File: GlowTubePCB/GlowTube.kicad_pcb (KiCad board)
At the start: 2 copper layers, 87.3 x 86.3 mm, 37 parts, among them J1 Conn_01x08, Q1 MMBT2222A, Q2 MMBT2222A, Q3 AP40P05, Q4 AP40P05, SW1 SW-SMD_4P-L3.7-W3.0-P1.50-LS4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, SW2 SW-SMD_4P-L3.7-W3.0-P1.50-LS4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, U1 ESP32-WROOM-32E (4MB), U2 PW14, U3 BL1117-33CX, U4 Val**

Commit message: updated pcb design
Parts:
- SW1, SW2: value SW-SMD_4P-L3.7-W3.0-P1.50-LS4.7 -> TS-1185EC-C-D-B
- U2: value PW14 -> SN74AHCT32QPWRQ1
- U4: value Val** -> CP2102-GMR
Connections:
- Q2 pad 2: RESET -> RTS
- Q2 pad 3: RTS -> RESET
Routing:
- net RESET: track 89.6 -> 88.2 mm
- net RTS: track 18.4 -> 17.7 mm
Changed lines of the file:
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@@
       (net 49 "Net-(Q2-Pad1)") (pintype "passive"))
     (pad "2" smd roundrect (at -0.9375 0.95 90) (size 1.475 0.6) (layers "F.Cu" "F.Paste" "F.Mask") (roundrect_rratio 0.25)
-      (net 4 "RESET") (pintype "passive"))
-    (pad "3" smd roundrect (at 0.9375 0 90) (size 1.475 0.6) (layers "F.Cu" "F.Paste" "F.Mask") (roundrect_rratio 0.25)
       (net 50 "RTS") (pintype "passive"))
+    (pad "3" smd roundrect (at 0.9375 0 90) (size 1.475 0.6) (layers "F.Cu" "F.Paste" "F.Mask") (roundrect_rratio 0.25)
+      (net 4 "RESET") (pintype "passive"))
     (model "${KICAD6_3DMODEL_DIR}/Package_TO_SOT_SMD.3dshapes/SOT-23.step"
       (offset (xyz 0 0 0))
@@
     (property "Sheetfile" "GlowTube.kicad_sch")
     (property "Sheetname" "")
-    (attr exclude_from_pos_files exclude_from_bom)
+    (attr exclude_from_pos_files)
     (fp_text reference "LED1" (at 0.1524 -3.5306 unlocked) (layer "F.SilkS") hide
       (effects (font (size 1 1) (thickness 0.15)))
@@
       (effects (font (size 1 1) (thickness 0.15)))
     )
-    (fp_text value "PW14" (at 0 0) (layer "F.SilkS") hide
+    (fp_text value "SN74AHCT32QPWRQ1" (at 0 0) (layer "F.SilkS") hide
       (effects (font (size 1 1) (thickness 0.15)))
     )
@@
     (property "Sheetfile" "GlowTube.kicad_sch")
     (property "Sheetname" "")
-    (attr through_hole exclude_from_pos_files exclude_from_bom)
+    (attr through_hole exclude_from_pos_files)
     (fp_text reference "J1" (at 0 -2.77) (layer "F.SilkS") hide
       (effects (font (size 1 1) (thickness 0.15)))
@@
       (effects (font (size 1 1) (thickness 0.15)) (justify right))
     )
-    (fp_text value "Val**" (at 0 0 90) (layer "F.SilkS") hide
+    (fp_text value "CP2102-GMR" (at 0 0 90) (layer "F.SilkS") hide
       (effects (font (size 1.27 1.27) (thickness 0.15)))
     )
@@
       (effects (font (size 1 1) (thickness 0.15)))
     )
-    (fp_text value "SW-SMD_4P-L3.7-W3.0-P1.50-LS4.7" (at 0 4.75) (layer "F.Fab")
+    (fp_text value "TS-1185EC-C-D-B" (at 0 4.75) (layer "F.Fab")
       (effects (font (size 1 1) (thickness 0.15)))
     )
@@
       (effects (font (size 1 1) (thickness 0.15)))
     )
-    (fp_text value "SW-SMD_4P-L3.7-W3.0-P1.50-LS4.7" (at 0 4.75) (layer "F.Fab")
+    (fp_text value "TS-1185EC-C-D-B" (at 0 4.75) (layer "F.Fab")
       (effects (font (size 1 1) (thickness 0.15)))
     )
@@
     (property "Sheetfile" "GlowTube.kicad_sch")
     (property "Sheetname" "")
-    (attr exclude_from_pos_files exclude_from_bom)
+    (attr exclude_from_pos_files)
     (fp_text reference "LED2" (at 0.1524 3.5306 unlocked) (layer "B.SilkS") hide
       (effects (font (size 1 1) (thickness 0.15)) (justify mirror))
@@
   (segment (start 114.34 161.6874) (end 113.2042 162.8232) (width 0.16) (layer "F.Cu") (net 4))
   (segment (start 112.7268 162.8232) (end 112.01 163.54) (width 0.16) (layer "F.Cu") (net 4))
+  (segment (start 142.5591 142.21) (end 142.5572 142.2081) (width 0.16) (layer "F.Cu") (net 4))
   (segment (start 115 160.5) (end 117.48 160.5) (width 0.16) (layer "F.Cu") (net 4))
   (segment (start 151.16 114.35) (end 149.5289 112.7189) (width 0.16) (layer "F.Cu") (net 4))
-  (segment (start 143.62 145.8) (end 143.5072 145.6872) (width 0.16) (layer "F.Cu") (net 4))
   (segment (start 114.34 161.16) (end 115 160.5) (width 0.16) (layer "F.Cu") (net 4))
   (segment (start 117.48 160.5) (end 118.14 161.16) (width 0.16) (layer "F.Cu") (net 4))
   (segment (start 114.34 161.16) (end 114.34 161.6874) (width 0.16) (layer "F.Cu") (net 4))
-  (segment (start 143.5072 145.6872) (end 143.5072 144.0831) (width 0.16) (layer "F.Cu") (net 4))
+  (segment (start 143.66 142.21) (end 142.5591 142.21) (width 0.16) (layer "F.Cu") (net 4))
   (segment (start 149.5289 112.7189) (end 149.5289 110.7052) (width 0.16) (layer "F.Cu") (net 4))
   (via (at 112.01 163.54) (size 0.8) (drill 0.4) (layers "F.Cu" "B.Cu") (net 4))
-  (via (at 143.62 145.8) (size 0.8) (drill 0.4) (layers "F.Cu" "B.Cu") (net 4))
+  (via (at 143.66 142.21) (size 0.8) (drill 0.4) (layers "F.Cu" "B.Cu") (net 4))
   (via (at 151.16 114.35) (size 0.8) (drill 0.4) (layers "F.Cu" "B.Cu") (net 4))
-  (segment (start 143.62 145.8) (end 143.62 131.29) (width 0.16) (layer "B.Cu") (net 4))
-  (segment (start 150.77 124.14) (end 151.16 123.75) (width 0.16) (layer "B.Cu") (net 4))
-  (segment (start 131.03 157.06) (end 142.29 145.8) (width 0.16) (layer "B.Cu") (net 4))
-  (segment (start 143.62 131.29) (end 150.77 124.14) (width 0.16) (layer "B.Cu") (net 4))
-  (segment (start 118.49 157.06) (end 131.03 157.06) (width 0.16) (layer "B.Cu") (net 4))
-  (segment (start 142.29 145.8) (end 143.62 145.8) (width 0.16) (layer "B.Cu") (net 4))
-  (segment (start 112.01 163.54) (end 118.49 157.06) (width 0.16) (layer "B.Cu") (net 4))
+  (segment (start 143.62 131.29) (end 151.16 123.75) (width 0.16) (layer "B.Cu") (net 4))
+  (segment (start 143.66 144.43) (end 131.03 157.06) (width 0.16) (layer "B.Cu") (net 4))
   (segment (start 151.16 123.75) (end 151.16 114.35) (width 0.16) (layer "B.Cu") (net 4))
+  (segment (start 143.66 142.21) (end 143.66 144.43) (width 0.16) (layer "B.Cu") (net 4))
+  (segment (start 143.62 142.17) (end 143.62 131.29) (width 0.16) (layer "B.Cu") (net 4))
+  (segment (start 143.66 142.21) (end 143.62 142.17) (width 0.16) (layer "B.Cu") (net 4))
+  (segment (start 118.49 157.06) (end 112.01 163.54) (width 0.16) (layer "B.Cu") (net 4))
+  (segment (start 131.03 157.06) (end 118.49 157.06) (width 0.16) (layer "B.Cu") (net 4))
   (segment (start 142.5842 107.010844) (end 142.5842 108.6442) (width 0.16) (layer "F.Cu") (net 9))
   (segment (start 142.5842 108.6442) (end 143.1789 109.2389) (width 0.16) (layer "F.Cu") (net 9))
@@
   (segment (start 133.210027 151.140001) (end 136.059999 151.140001) (width 0.16) (layer "F.Cu") (net 48))
   (segment (start 140.69 146.51) (end 140.69 144.8981) (width 0.16) (layer "F.Cu") (net 48))
-  (segment (start 141.7425 143.9478) (end 141.7425 140.25) (width 0.16) (layer "F.Cu") (net 49))
   (segment (start 141.6072 144.0831) (end 141.7425 143.9478) (width 0.16) (layer "F.Cu") (net 49))
+  (segment (start 141.6072 140.3853) (end 141.7425 140.25) (width 0.16) (layer "F.Cu") (net 49))
+  (segment (start 141.6072 144.0831) (end 141.6072 140.3853) (width 0.16) (layer "F.Cu") (net 49))
   (segment (start 142.65 147.11) (end 142.65 147.0757) (width 0.16) (layer "F.Cu") (net 50))
-  (segment (start 142.5572 145.0487) (end 141.5901 146.0158) (width 0.16) (layer "F.Cu") (net 50))
-  (segment (start 142.5572 142.2081) (end 142.5572 145.0487) (width 0.16) (layer "F.Cu") (net 50))
+  (segment (start 143.5072 145.4328) (end 143.5072 144.0831) (width 0.16) (layer "F.Cu") (net 50))
+  (segment (start 141.5901 146.0158) (end 141.7059 145.9) (width 0.16) (layer "F.Cu") (net 50))
   (segment (start 137.73 153.14) (end 133.210027 153.14) (width 0.16) (layer "F.Cu") (net 50))
   (segment (start 141.39 149.64) (end 141.23 149.64) (width 0.16) (layer "F.Cu") (net 50))
   (segment (start 142.65 147.0757) (end 141.5901 146.0158) (width 0.16) (layer "F.Cu") (net 50))
   (segment (start 141.23 149.64) (end 137.73 153.14) (width 0.16) (layer "F.Cu") (net 50))
+  (segment (start 143.04 145.9) (end 143.5072 145.4328) (width 0.16) (layer "F.Cu") (net 50))
+  (segment (start 141.7059 145.9) (end 143.04 145.9) (width 0.16) (layer "F.Cu") (net 50))
   (via (at 142.65 147.11) (size 0.8) (drill 0.4) (layers "F.Cu" "B.Cu") (net 50))
   (via (at 141.39 149.64) (size 0.8) (drill 0.4) (layers "F.Cu" "B.Cu") (net 50))

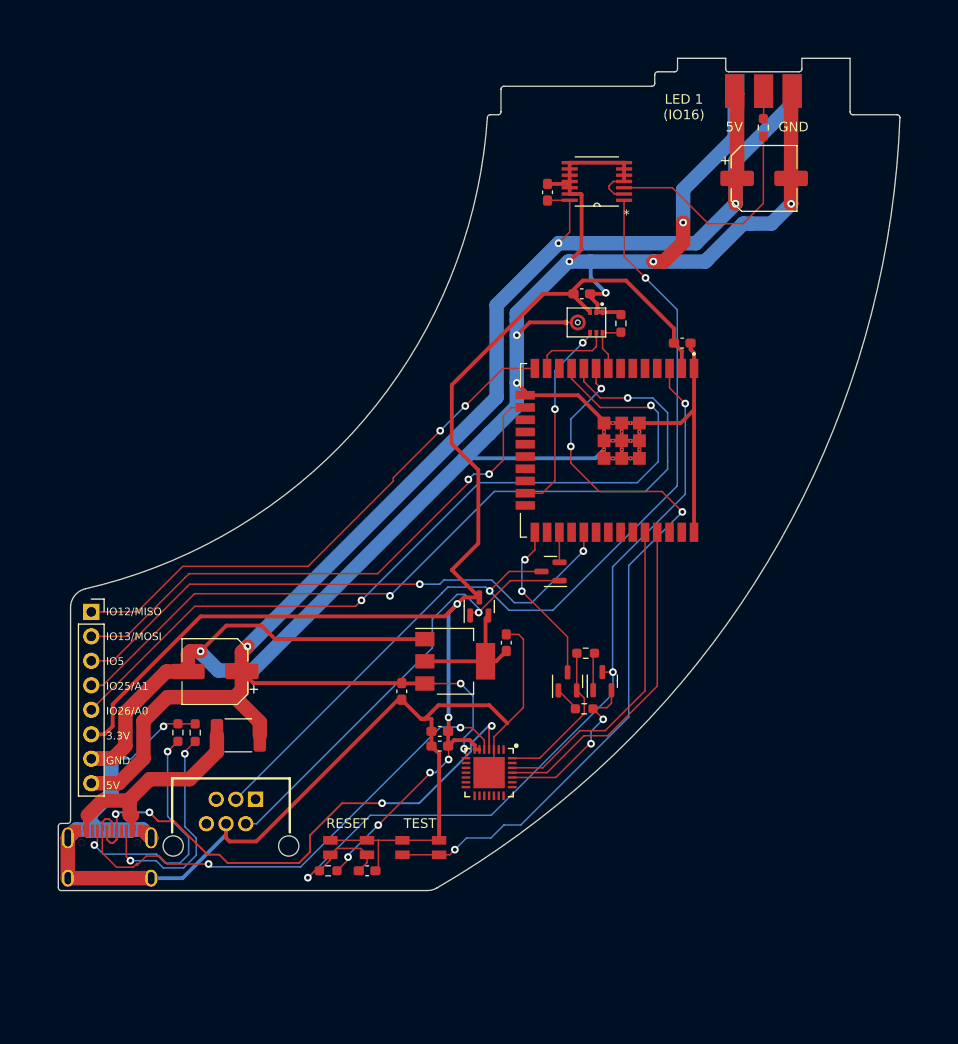
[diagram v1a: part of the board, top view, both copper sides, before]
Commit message: redesigned GlowTube PCBs
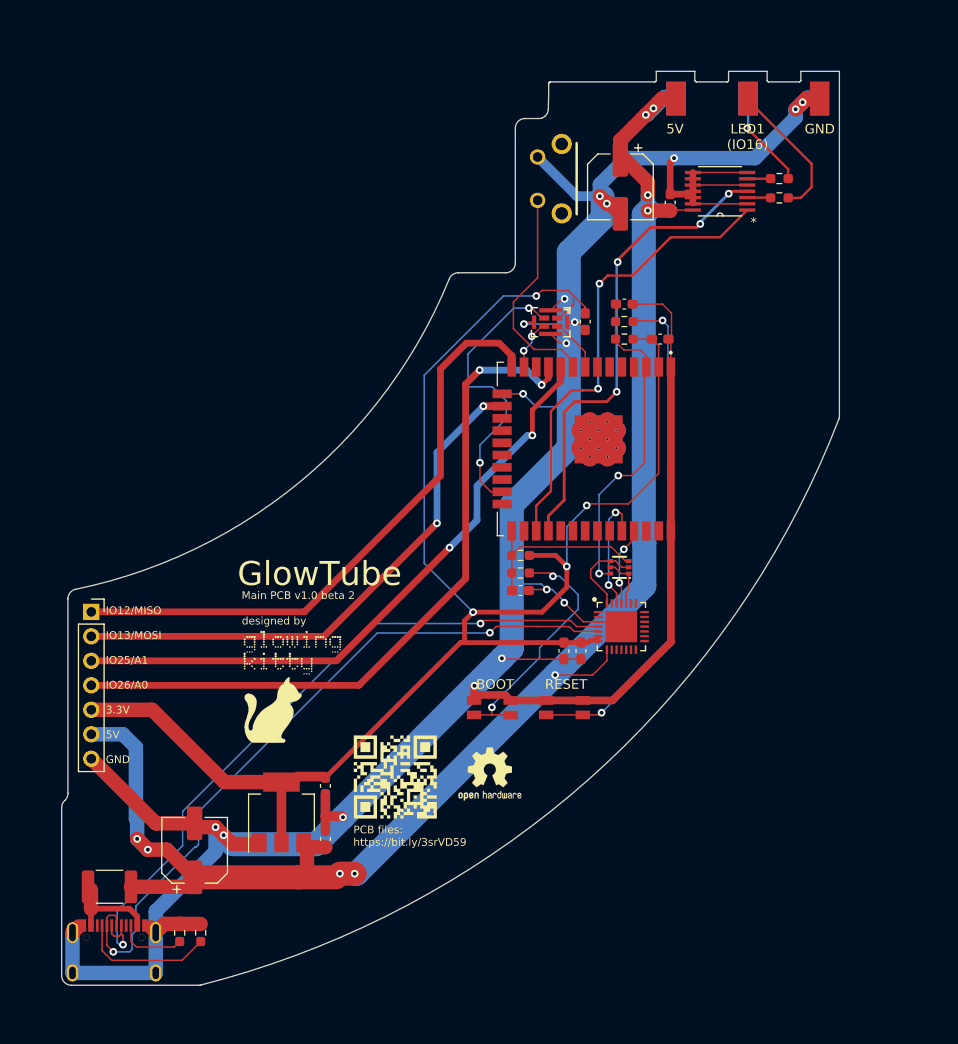
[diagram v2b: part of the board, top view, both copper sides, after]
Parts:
- removed LED1, LED2: LED_strip_contact_pads, Connector:LED strip connector pad
- removed MK1: ICS-43432, ICS-43432:MIC_ICS-43432
- removed Q1, Q2: MMBT2222A, Package_TO_SOT_SMD:SOT-23
- removed Q3, Q4: AP40P05, Package_TO_SOT_SMD:SOT-23
- removed REF**: OSHW-Logo2_7.3x6mm_SilkScreen, Symbol:OSHW-Logo2_7.3x6mm_SilkScreen
- removed RJ1: R-RJ11R06P-A800, R-RJ11R06P-A800:R-RJ11R06P-A800
- added C11: 1nF, Capacitor_SMD:C_0603_1608Metric_Pad1.08x0.95mm_HandSolder, F.Cu at (134.1, 133.7)
- added C12: KAN0637-0701B, footprint:SW-TH_KAN0637-0701B, F.Cu at (134.9, 91.0)
- added OSHW logo: OSHW-Logo2_7.3x6mm_SilkScreen, Symbol:OSHW-Logo2_7.3x6mm_SilkScreen, F.Cu at (130.9, 152.8)
- added P1: Solder_Pad, footprint:Solder pad, F.Cu at (150.3, 82.7)
- added P2: Solder_Pad, footprint:Solder pad, F.Cu at (157.8, 82.7)
- added P3: Solder_Pad, footprint:Solder pad, F.Cu at (165.2, 82.7)
- added P4: Solder_Pad, footprint:Solder pad, B.Cu at (150.1, 82.7)
- added P5: Solder_Pad, footprint:Solder pad, B.Cu at (165.0, 82.7)
- added P6: Solder_Pad, footprint:Solder pad, B.Cu at (157.6, 82.7)
- added R8: 62, Resistor_SMD:R_0603_1608Metric_Pad0.98x0.95mm_HandSolder, F.Cu at (160.9, 91.0)
- added U5: UMH3N, footprint:SC-70-6_L2.2-W1.3-P0.65-LS2.1-BR, F.Cu at (144.3, 131.3)
- added U6: GMA4030H11-F26, GMA4030H11-F26:GMA4030H11-F26, F.Cu at (137.2, 105.9)
- C1: value 220uF 10V -> 10uF; footprint Capacitor_SMD:CP_Elec_6.3x5.4 -> Capacitor_SMD:C_0603_1608Metric_Pad1.08x0.95mm_HandSolder
- C10: value 1uF -> 1nF
- C3: value 10uF -> 220uF 10V; footprint Capacitor_SMD:C_0603_1608Metric_Pad1.08x0.95mm_HandSolder -> Capacitor_SMD:CP_Elec_6.3x5.4
- C4: value 4.7uF 6.3V 10% -> 220uF 10V; footprint Capacitor_SMD:C_0603_1608Metric_Pad1.08x0.95mm_HandSolder -> Capacitor_SMD:CP_Elec_6.3x5.4
- C5: value 10uF -> 4.7uF 6.3V 10%
- C8: value 0.1uF -> 10uF
- C9: value 220uF 10V -> 0.1uF; footprint Capacitor_SMD:CP_Elec_6.3x5.4 -> Capacitor_SMD:C_0603_1608Metric_Pad1.08x0.95mm_HandSolder
- G*** (x2): moved to F.Cu
- J1: value Conn_01x08 -> Conn_01x07; footprint Connector_PinSocket_2.54mm:PinSocket_1x08_P2.54mm_Vertical -> Connector_PinSocket_2.54mm:PinSocket_1x07_P2.54mm_Vertical
- R4, R5: value 10K -> 220
- R6: value 100K -> 10K
- U1: value ESP32-WROOM-32E (4MB) -> SN74AHCT32QPWRQ1; footprint ESP32-WROOM-32E__16MB_:MODULE_ESP32-WROOM-32E_(16MB) -> SN74AHCT32QPWRQ1:SN74AHCT32QPWRQ1
- U2: value SN74AHCT32QPWRQ1 -> ESP32-WROOM-32E (4MB); footprint SN74AHCT32QPWRQ1:SN74AHCT32QPWRQ1 -> ESP32-WROOM-32E__16MB_:MODULE_ESP32-WROOM-32E_(16MB)
- U3: value BL1117-33CX -> CP2102-GMR; footprint Package_TO_SOT_SMD:SOT-223 -> CP2102-GMR:CP2102-GMR
- U4: value CP2102-GMR -> BL1117-33CX; footprint CP2102-GMR:CP2102-GMR -> Package_TO_SOT_SMD:SOT-223
- moved C10 64.6 mm to (144.8, 104.0), turned to 0 degrees
- moved C4 61.0 mm to (144.4, 91.9), turned to -90 degrees
- moved C1 57.6 mm to (148.6, 107.7)
- moved C8 57.6 mm to (113.8, 154.0), turned to 90 degrees
- moved R4 40.4 mm to (144.8, 105.8)
- moved R7 38.3 mm to (134.1, 130.1)
- moved C5 33.6 mm to (140.3, 140.0), turned to 90 degrees
- moved U1 28.0 mm to (154.8, 92.3), turned to 180 degrees
- moved U2 27.9 mm to (144.4, 119.1), turned to -90 degrees
- moved C7 27.7 mm to (113.8, 159.5)
- moved G*** 27.5 mm to (110.3, 142.7), turned to 0 degrees
- moved C3 27.1 mm to (100.3, 160.7)
- moved C9 23.8 mm to (140.8, 105.9), turned to 90 degrees
- moved U4 21.9 mm to (109.3, 156.8), turned to 90 degrees
- moved R2 20.9 mm to (100.9, 169.2)
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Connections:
- net Net-(F1-Pad1) renamed VBUS
- C1 pad 1: +5V -> GND
- C1 pad 2: GND -> +3V3
- C10 pad 1: GND -> RESET
- C10 pad 2: RESET -> GND
- C3 pad 1: GND -> +5V
- C3 pad 2: +5V -> GND
- C4 pad 1: GND -> +5V
- C4 pad 2: +3V3 -> GND
- C5 pad 1: +3V3 -> GND
- C5 pad 2: GND -> +3V3
- C7 pad 2: Net-(C7-Pad2) -> +5V
- C9 pad 1: +5V -> GND
- C9 pad 2: GND -> +3V3
- J1 pad 1: IO12 -> IO12/MISO
- J1 pad 2: IO13 -> IO13/MOSI
- J1 pad 3: IO5 -> IO25/A1/DAC1
- J1 pad 4: IO25/A1/DAC1 -> IO26/A0/DAC2
- J1 pad 5: IO26/A0/DAC2 -> +3V3
- J1 pad 6: +3V3 -> +5V
- R4 pad 1: RTS -> Net-(R4-Pad1)
- R4 pad 2: Net-(Q1-Pad1) -> RESET
- R5 pad 1: DTR -> Net-(R5-Pad1)
- R5 pad 2: Net-(Q2-Pad1) -> IO0
- R6 pad 1: IO32/SD -> RESET
- R6 pad 2: GND -> +3V3
- R7 pad 1: RESET -> IO0
- SW1 pad 2: IO33/TESTBUTTON -> Net-(R4-Pad1)
- SW2 pad 2: RESET -> Net-(R5-Pad1)
- U1 pad 1: GND -> IO16/LED1
- U1 pad 10: IO25/A1/DAC1 -> GND
- U1 pad 11: IO26/A0/DAC2 -> GND
- U1 pad 12: IO27 -> GND
- U1 pad 13: IO14/SCK -> GND
- U1 pad 14: IO12 -> +5V
- U1 pad 2: +3V3 -> GND
- U1 pad 3: RESET -> Net-(R1-Pad1)
- U1 pad 4: IO36/A4/SENSOR_VP -> IO17/LED2
- U1 pad 5: I39/A3/SENSOR_VN -> GND
- U1 pad 6: I34/A2 -> Net-(U1-Pad6)
- U1 pad 7: IO35 -> GND
- U1 pad 8: IO32/SD -> GND
- U1 pad 9: IO33/TESTBUTTON -> GND
- U2 pad 1: LED1 DATA IN -> GND
- U2 pad 10: GND -> IO25/A1/DAC1
- U2 pad 11: GND -> IO26/A0/DAC2
- U2 pad 12: GND -> IO27
- U2 pad 13: GND -> IO14/SCK
- U2 pad 14: +5V -> IO12/MISO
- U2 pad 2: GND -> +3V3
- U2 pad 3: Net-(R1-Pad1) -> RESET
- U2 pad 4: GND -> IO36/A4/SENSOR_VP
- U2 pad 5: GND -> I39/A3/SENSOR_VN
- U2 pad 6: GND -> I34/A2
- U2 pad 7: GND -> IO35
- U2 pad 8: GND -> IO32/SD
- U2 pad 9: GND -> IO33/MAINBUTTON
- U3 pad 1: GND -> unconnected-(U3-Pad1)
- U3 pad 2: Net-(C7-Pad2) -> unconnected-(U3-Pad2)
- U3 pad 3: +5V -> GND
- U3 pad 4: Net-(C7-Pad2) -> USB-C DATA+
- U4 pad 1: unconnected-(U4-Pad1) -> GND
- U4 pad 2: unconnected-(U4-Pad2) -> +3V3
- U4 pad 3: GND -> +5V
- U4 pad 4: USB-C DATA+ -> +3V3
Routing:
- net LED1 DATA IN: track 99.4 -> 0.00 mm, vias 2 -> 0
- net IO33/TESTBUTTON: track 78.0 -> 0.00 mm, vias 4 -> 0
- net GND: track 427.0 -> 354.9 mm, vias 9 -> 17
- net IO12/MISO: track 0.00 -> 63.4 mm
- net IO5: track 59.7 -> 0.00 mm, vias 2 -> 0
- net IO13: track 57.8 -> 0.00 mm, vias 2 -> 0
- net IO13/MOSI: track 0.00 -> 56.8 mm, vias 0 -> 2
- net IO12: track 56.7 -> 0.00 mm, vias 2 -> 0
- net RESET: track 88.2 -> 34.3 mm, vias 3 -> 2
- net Net-(R4-Pad1): track 0.00 -> 52.7 mm, vias 0 -> 2
- net IO17/LED2: track 0.00 -> 49.6 mm, vias 0 -> 4
- net RECEIVER 5V: track 47.6 -> 0.00 mm, vias 1 -> 0
- net IO16/LED1: track 3.12 -> 48.4 mm, vias 0 -> 2
- net TXD0: track 34.7 -> 8.26 mm, vias 0 -> 2
- net +3V3: track 147.3 -> 173.4 mm, vias 6 -> 4
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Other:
- board size 87.3 x 86.3 mm -> 80.7 x 94.8 mm
- board text added: "BOOT"
- board text added: "IO12/MISO IO13/MOSI IO25/A1 IO26/A0 3.3V 5V GND"
- board text added: "LED1 (IO16)"
- board text added: "LED2 (IO17)"
- board text added: "Main PCB v1.0 beta 2"
- board text removed: "IO12/MISO IO13/MOSI IO5 IO25/A1 IO26/A0 3.3V GND 5V"
- board text removed: "LED 1 (IO16)"
- board text removed: "TEST"
- board text removed: "v1.0 beta 1"

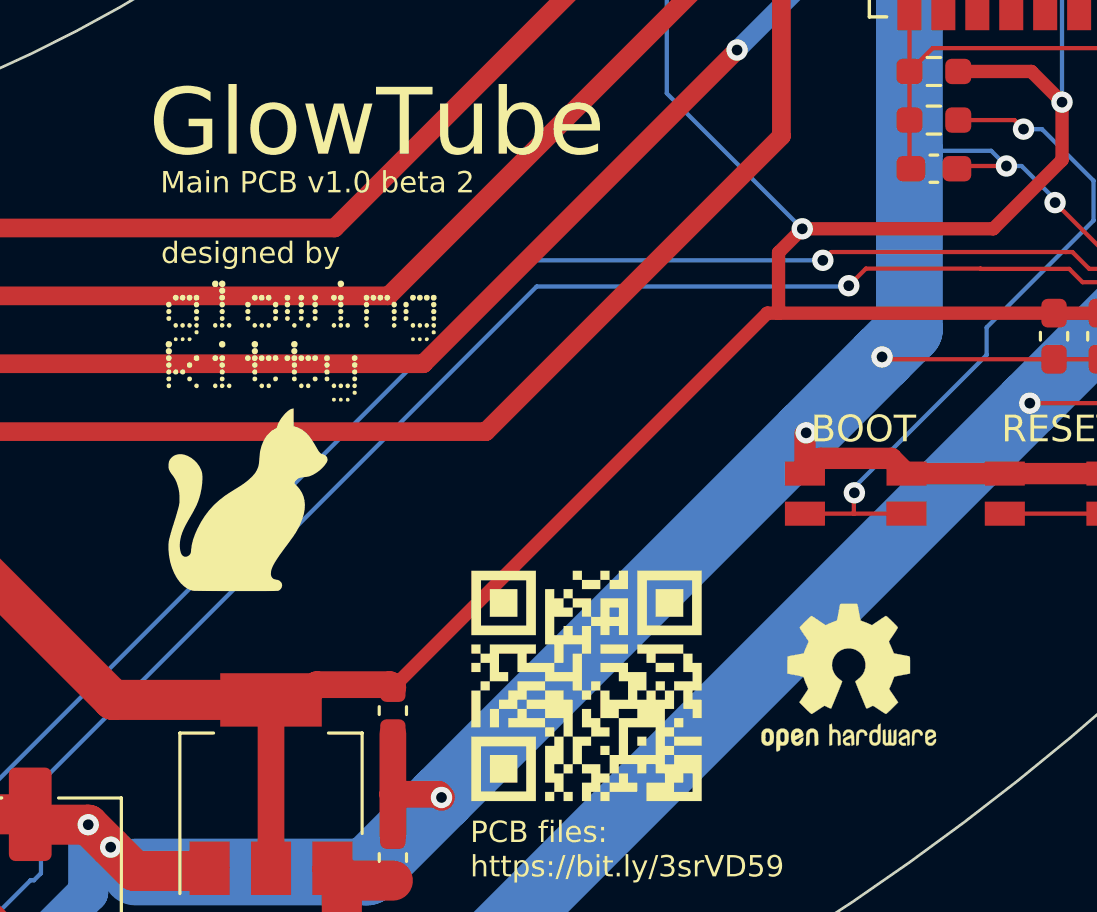
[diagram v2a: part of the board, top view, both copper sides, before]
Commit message: updated 3d model and software upload fix
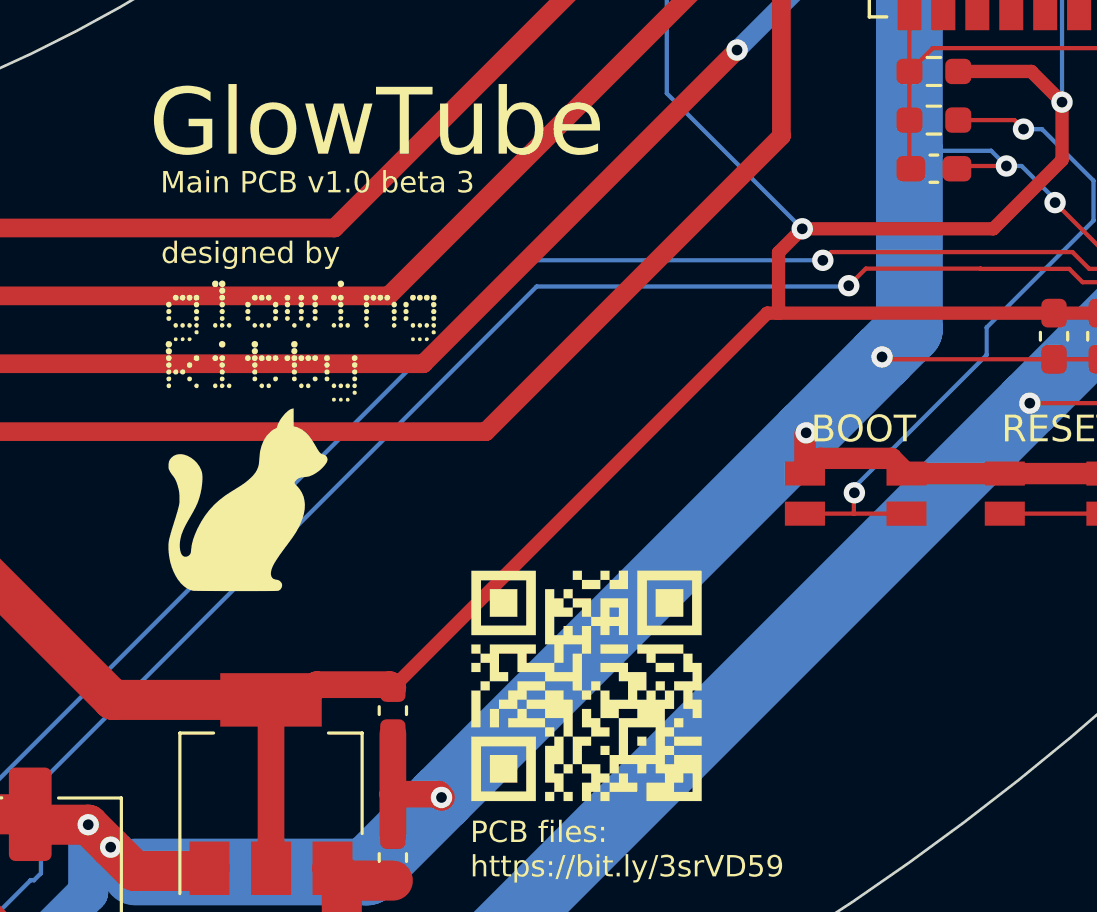
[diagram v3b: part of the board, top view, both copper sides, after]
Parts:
- removed OSHW logo: OSHW-Logo2_7.3x6mm_SilkScreen, Symbol:OSHW-Logo2_7.3x6mm_SilkScreen
- C10, C11: value 1nF -> 1uF
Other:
- board text added: "Main PCB v1.0 beta 3"
- board text removed: "Main PCB v1.0 beta 2"
